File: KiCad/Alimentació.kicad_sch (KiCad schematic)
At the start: 9 parts, among them J1 Conn_01x02

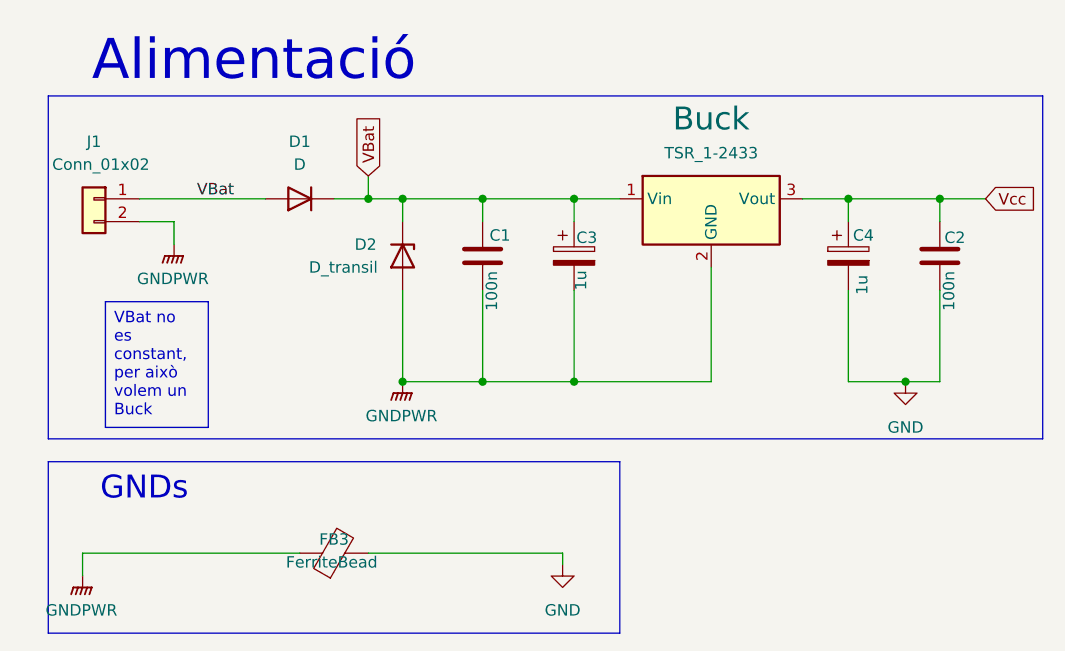
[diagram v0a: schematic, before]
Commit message: Microprocessador finalissim + placement de alimentacion y micro
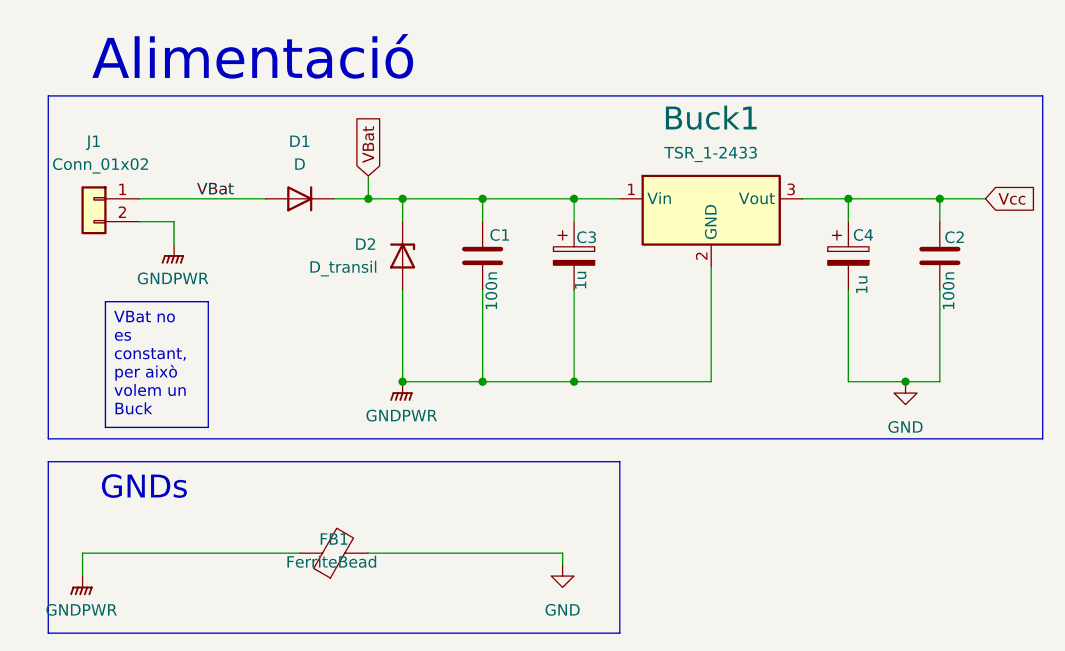
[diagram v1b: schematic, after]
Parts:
- C1, C2: footprint (none) -> Capacitor_SMD:C_0805_2012Metric_Pad1.18x1.45mm_HandSolder
- C3, C4: footprint (none) -> Capacitor_SMD:CP_Elec_4x5.7
- D1: footprint (none) -> Capacitor_SMD:C_1812_4532Metric_Pad1.57x3.40mm_HandSolder
- D2: footprint (none) -> Diode_THT:D_DO-35_SOD27_P2.54mm_Vertical_AnodeUp
- FB1: renamed from FB3; footprint (none) -> Ferrite_THT:LairdTech_28C0236-0JW-10
- J1: footprint (none) -> Connector_AMASS:AMASS_XT60-M_1x02_P7.20mm_Vertical
- renumbered Buck to Buck1
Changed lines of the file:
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@@
 			)
 		)
-		(property "Footprint" ""
+		(property "Footprint" "Connector_AMASS:AMASS_XT60-M_1x02_P7.20mm_Vertical"
 			(at 24.13 39.37 0)
 			(effects
@@
 		(on_board yes)
 		(dnp no)
-		(property "Reference" "FB3"
+		(property "Reference" "FB1"
 			(at 50.8 77.216 90)
 			(effects
@@
 			)
 		)
-		(property "Footprint" ""
+		(property "Footprint" "Ferrite_THT:LairdTech_28C0236-0JW-10"
 			(at 50.8 80.518 90)
 			(effects
@@
 			(project "Retrovisors_Carlos_Soler_Ingrid_Lopez"
 				(path "/a9cf8edd-cd44-4958-b775-951afc8c27af/d3554d12-72fa-4385-8426-b60739af6be0"
-					(reference "FB3")
+					(reference "FB1")
 					(unit 1)
 				)
@@
 			)
 		)
-		(property "Footprint" ""
+		(property "Footprint" "Capacitor_SMD:CP_Elec_4x5.7"
 			(at 78.4352 49.53 0)
 			(effects
@@
 			)
 		)
-		(property "Footprint" ""
+		(property "Footprint" "Capacitor_SMD:C_0805_2012Metric_Pad1.18x1.45mm_HandSolder"
 			(at 68.2752 49.53 0)
 			(effects
@@
 			)
 		)
-		(property "Footprint" ""
+		(property "Footprint" "Diode_THT:D_DO-35_SOD27_P2.54mm_Vertical_AnodeUp"
 			(at 58.42 45.72 0)
 			(effects
@@
 			)
 		)
-		(property "Footprint" ""
+		(property "Footprint" "Capacitor_SMD:C_0805_2012Metric_Pad1.18x1.45mm_HandSolder"
 			(at 119.0752 49.53 0)
 			(effects
@@
 		(dnp no)
 		(fields_autoplaced yes)
-		(property "Reference" "Buck"
+		(property "Reference" "Buck1"
 			(at 92.71 30.48 0)
 			(effects
@@
 			(project "Retrovisors_Carlos_Soler_Ingrid_Lopez"
 				(path "/a9cf8edd-cd44-4958-b775-951afc8c27af/d3554d12-72fa-4385-8426-b60739af6be0"
-					(reference "Buck")
+					(reference "Buck1")
 					(unit 1)
 				)
@@
 			)
 		)
-		(property "Footprint" ""
+		(property "Footprint" "Capacitor_SMD:C_1812_4532Metric_Pad1.57x3.40mm_HandSolder"
 			(at 46.99 39.37 0)
 			(effects
@@
 			)
 		)
-		(property "Footprint" ""
+		(property "Footprint" "Capacitor_SMD:CP_Elec_4x5.7"
 			(at 108.9152 49.53 0)
 			(effects
